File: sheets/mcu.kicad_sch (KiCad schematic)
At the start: 37 parts, among them SW1 SW_Push, SW2 SW_SPST, U1 STM32H755ZIT6, Y1 25M, Y2 32k768

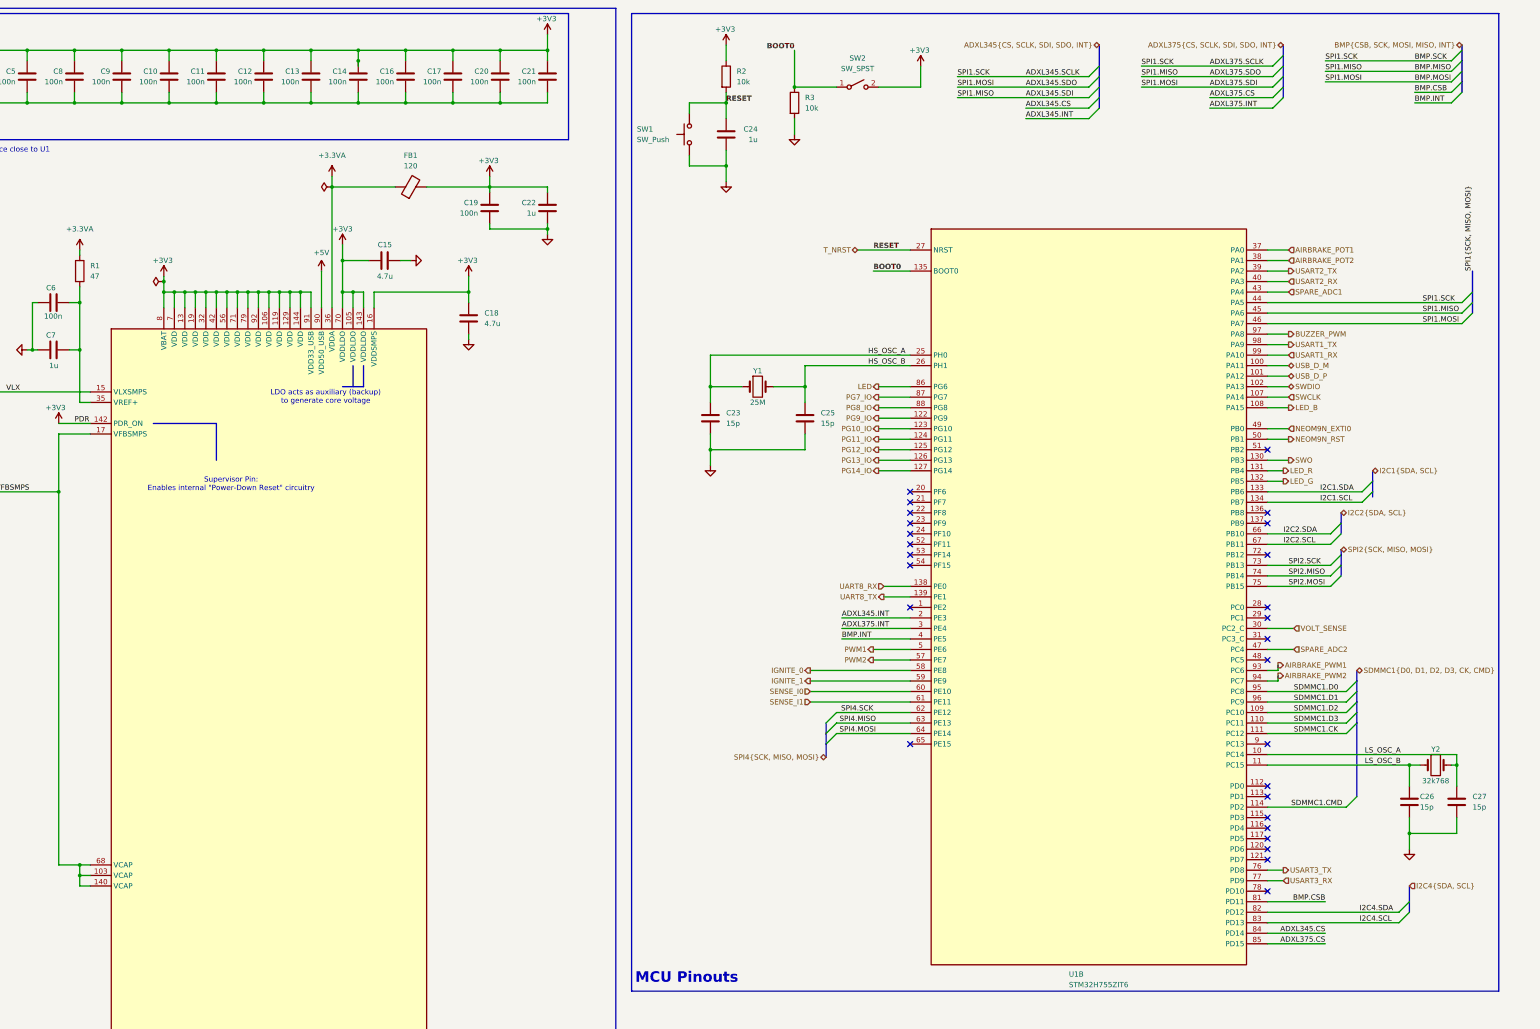
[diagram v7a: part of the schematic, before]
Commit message: Cleared ALL ERC warnings
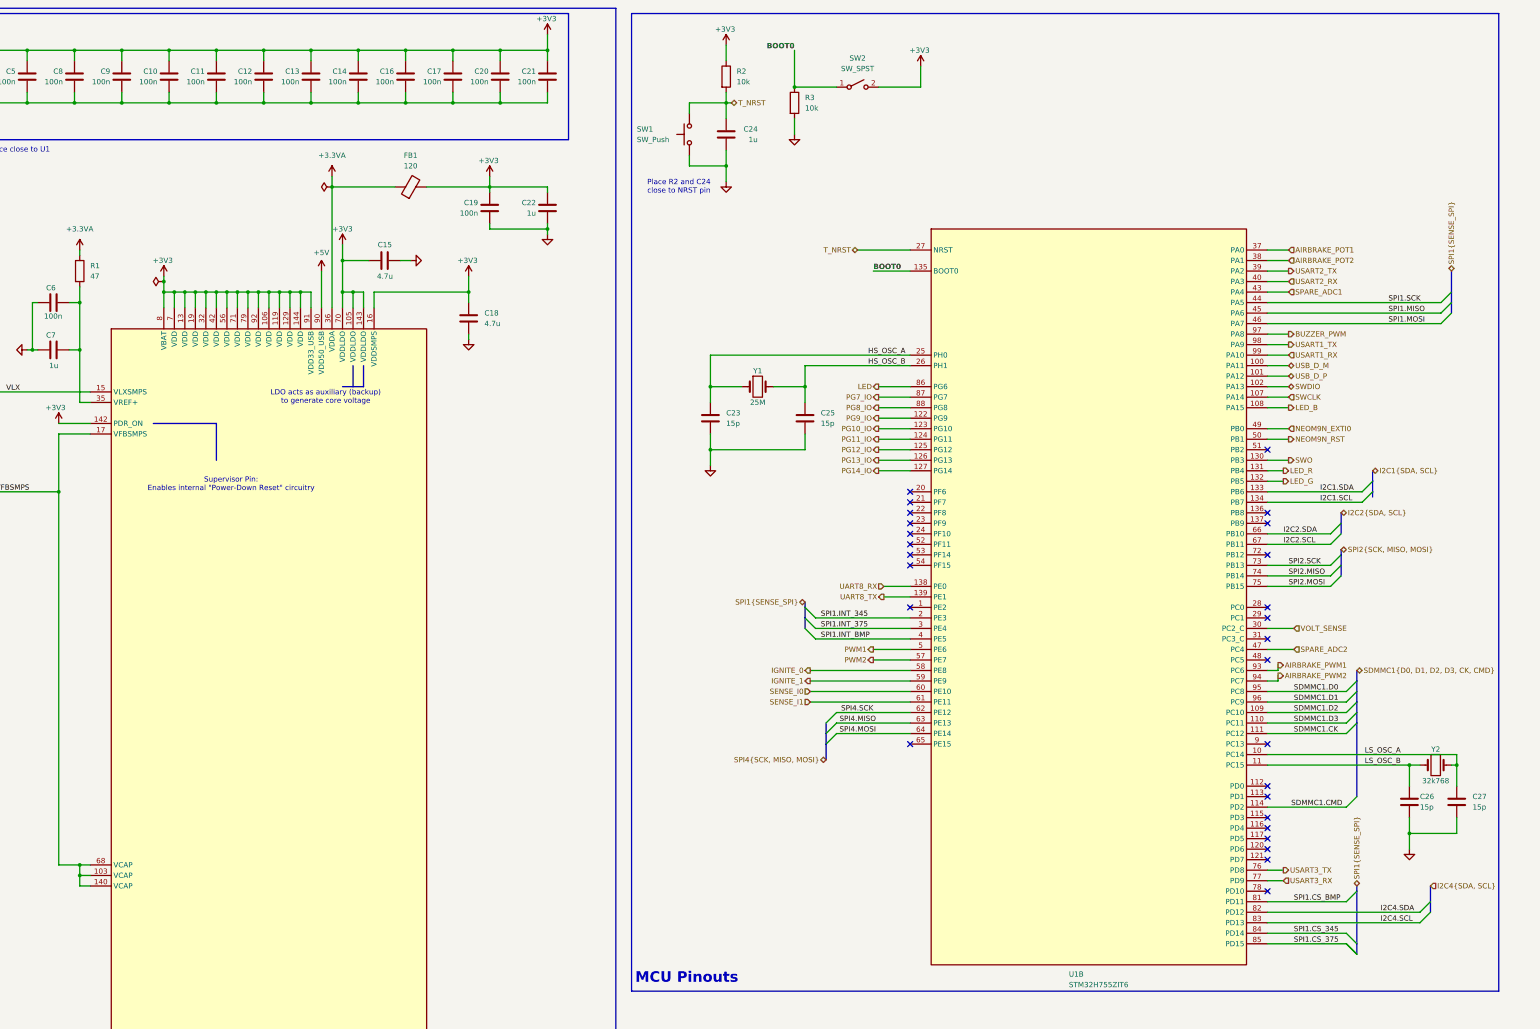
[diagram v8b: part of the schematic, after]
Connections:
- net ADXL345.CS renamed SPI1.CS_345
- net ADXL345.INT renamed SPI1.INT_345
- net ADXL345.SCLK renamed SPI1.SCK
- net ADXL345.SDI renamed SPI1.MISO
- net ADXL345.SDO renamed SPI1.MOSI
- net ADXL375.CS renamed SPI1.CS_375
- net ADXL375.INT renamed SPI1.INT_375
- net BMP.CSB renamed SPI1.CS_BMP
- net BMP.INT renamed SPI1.INT_BMP
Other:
- note added: "Place R2 and C24 close to NRST pin"
